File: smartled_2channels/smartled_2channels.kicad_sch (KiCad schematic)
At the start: 80 parts, among them J1 Conn_01x04, J2 Conn_01x02, SW1 SW_Push, U1 OC5028B, U2 MAX485E, U3 PY32F003F1xUx, U4 OC5864, U5 SGM2033-3.3, U6 OC5028B, U7 GS8521

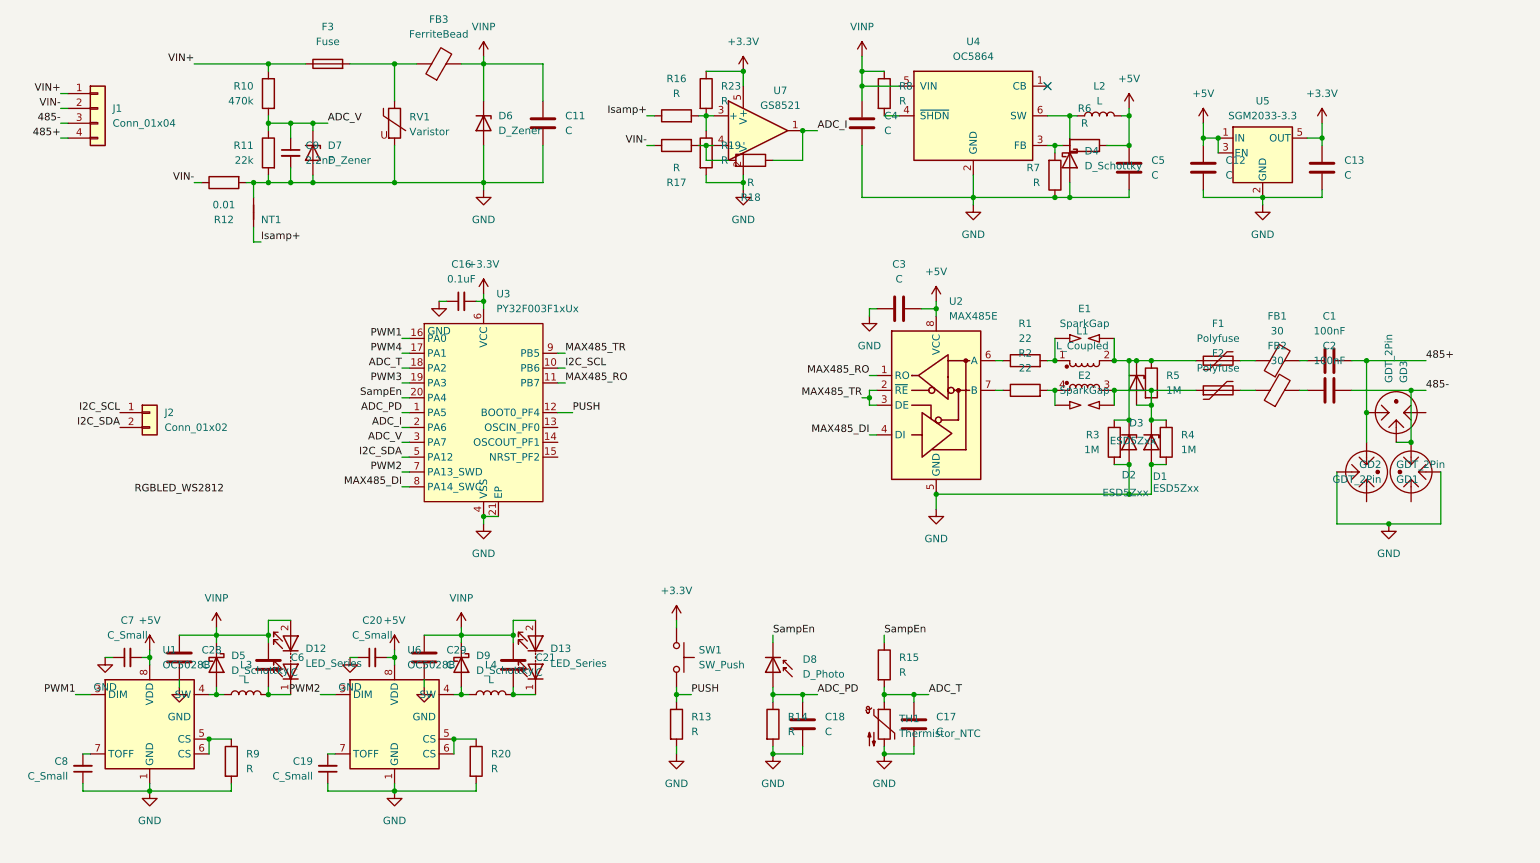
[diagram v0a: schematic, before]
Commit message: 添加麦克风声感应电路，红外和雷达传感器接口
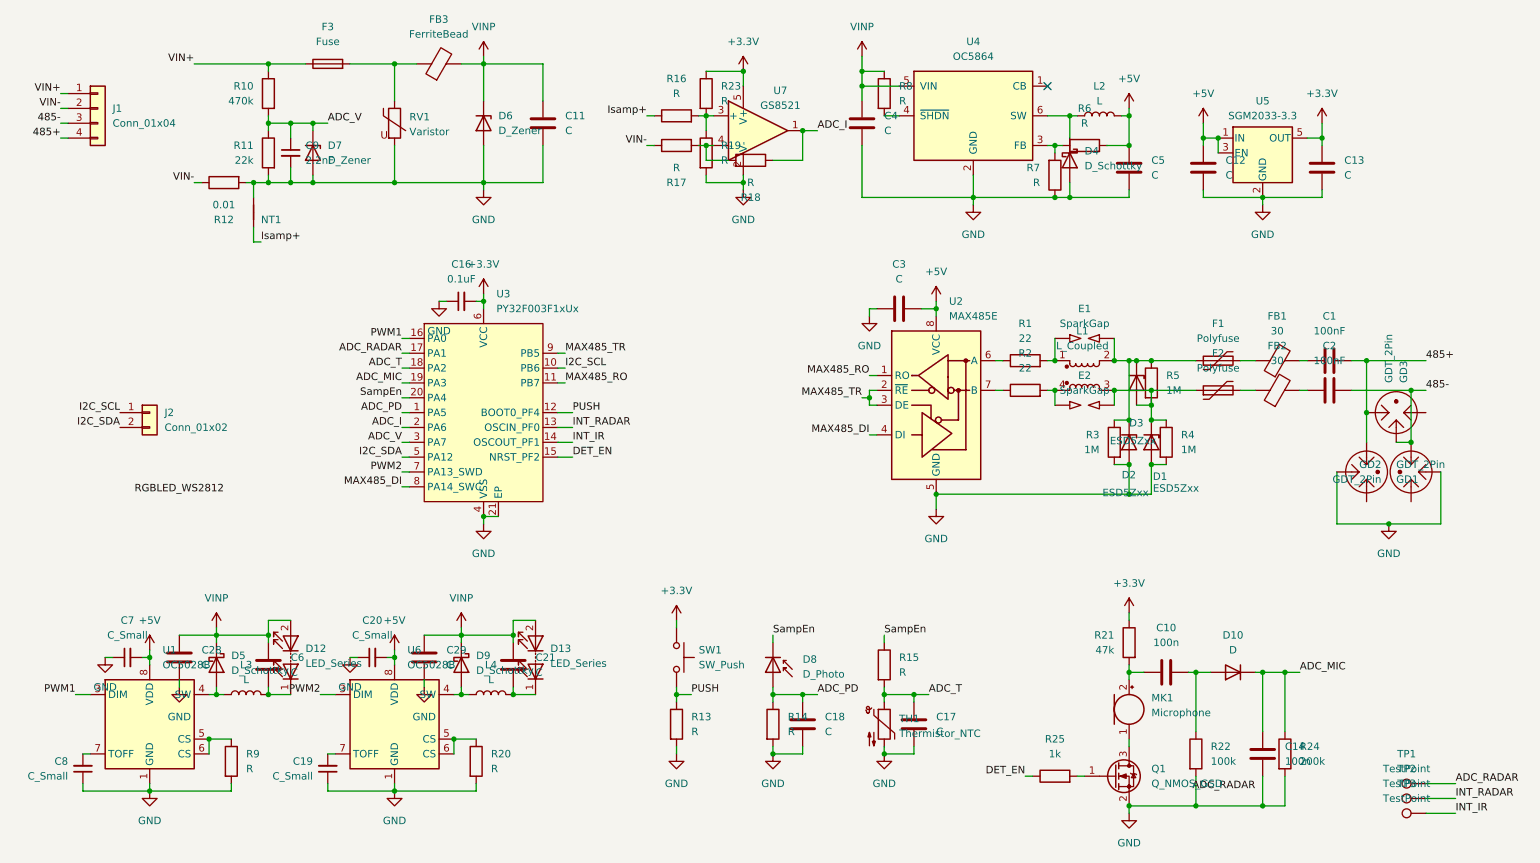
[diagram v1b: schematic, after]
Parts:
- added C10, C14: 100n, Capacitor_SMD:C_0402_1005Metric, symbol Device:C
- added D10: D, Diode_SMD:D_SOD-523, symbol Device:D
- added MK1: Microphone, Diode_SMD:D_SOD-123F, symbol Device:Microphone
- added Q1: Q_NMOS_GSD, Package_TO_SOT_SMD:SOT-23, symbol Device:Q_NMOS_GSD
- added R21: 47k, Resistor_SMD:R_0402_1005Metric, symbol Device:R
- added R22: 100k, Resistor_SMD:R_0402_1005Metric, symbol Device:R
- added R24: 200k, Resistor_SMD:R_0402_1005Metric, symbol Device:R
- added R25: 1k, Resistor_SMD:R_0402_1005Metric, symbol Device:R
- added TP1, TP2, TP3: TestPoint, TestPoint:TestPoint_Pad_D1.0mm, symbol Connector:TestPoint
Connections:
- net +3.3V: now also R21.1
- net GND: now also C14.2, Q1.2 (S), R22.2, R24.2
- net INT_RADAR: now reaches U3.13 (OSCIN_PF0)
- net INT_RADAR: now also TP2.1
- net INT_IR: now reaches U3.14 (OSCOUT_PF1)
- net INT_IR: now also TP3.1
- net DET_EN: now reaches U3.15 (NRST_PF2)
- net DET_EN: now also R25.1
- net PWM3 renamed ADC_MIC
- net ADC_MIC: now also C14.1, D10.1 (K), R24.1
- net PWM4 renamed ADC_RADAR
- net ADC_RADAR: now also TP1.1
- new net: Q1.1 (G), R25.2
- new net: C10.1, MK1.2 (+), R21.2
- new net: MK1.1 (-), Q1.3 (D)
- new net: C10.2, D10.2 (A), R22.1

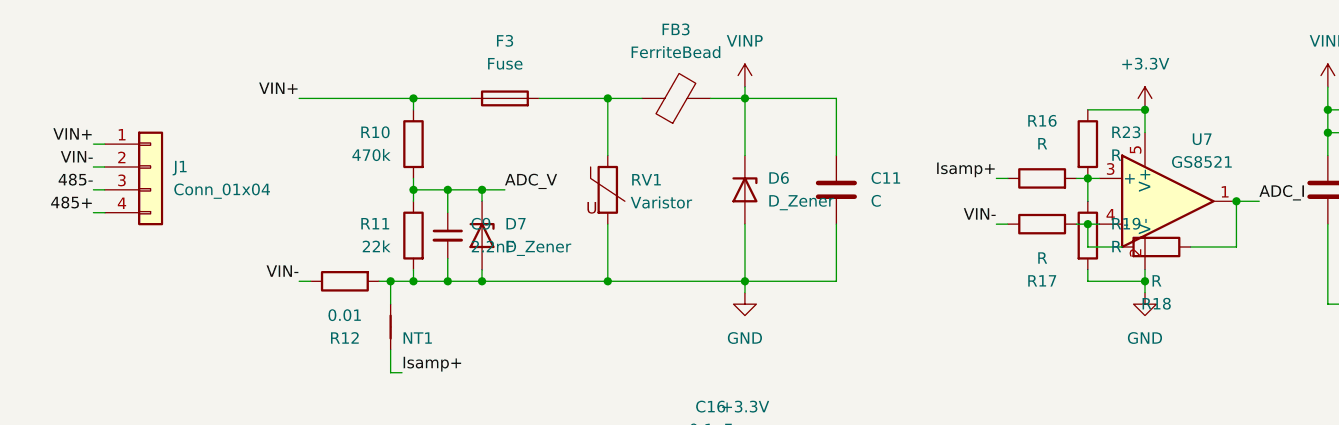
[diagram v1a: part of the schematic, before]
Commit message: 进行布线，微调原理图
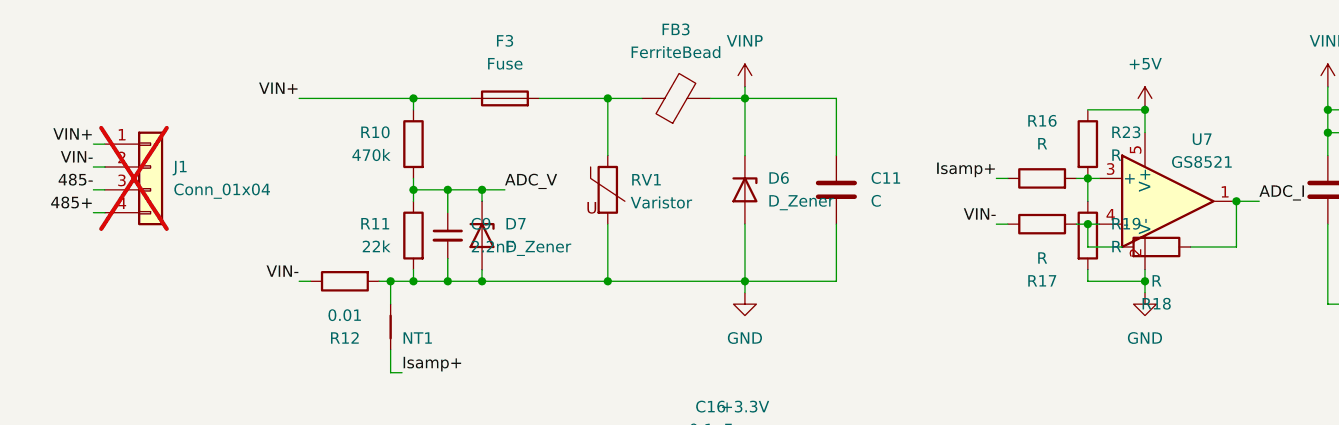
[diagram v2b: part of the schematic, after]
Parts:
- D7, MK1: footprint Diode_SMD:D_SOD-123F -> Diode_SMD:D_SOD-323
- F3: footprint project_footprints:Fuse_2410_6125Metric -> Fuse:Fuse_1206_3216Metric
- J1: now not fitted
- R22: footprint Resistor_SMD:R_0402_1005Metric -> Resistor_SMD:R_0603_1608Metric
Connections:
- net +3.3V: no longer R23.1, U7.5 (V+)
- net +5V: now also R23.1, U7.5 (V+)
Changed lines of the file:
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@@
 	)
 	(junction
-		(at 203.2 80.01)
+		(at 139.7 30.48)
 		(diameter 0)
 		(color 0 0 0 0)
 	)
 	(junction
-		(at 139.7 30.48)
+		(at 203.2 80.01)
 		(diameter 0)
 		(color 0 0 0 0)
@@
 			)
 		)
-		(property "Footprint" "Diode_SMD:D_SOD-123F"
+		(property "Footprint" "Diode_SMD:D_SOD-323"
 			(at 205.74 137.16 90)
 			(effects
@@
 			)
 		)
-		(property "Footprint" "Resistor_SMD:R_0402_1005Metric"
+		(property "Footprint" "Resistor_SMD:R_0603_1608Metric"
 			(at 215.392 147.32 90)
 			(effects
@@
 			)
 		)
-		(property "Footprint" "Diode_SMD:D_SOD-123F"
+		(property "Footprint" "Diode_SMD:D_SOD-323"
 			(at 66.04 44.45 0)
 			(effects
@@
 		(exclude_from_sim no)
 		(in_bom yes)
-		(on_board yes)
-		(dnp no)
+		(on_board no)
+		(dnp yes)
 		(fields_autoplaced yes)
 		(property "Reference" "J1"
@@
 			)
 		)
-		(property "Footprint" "project_footprints:Fuse_2410_6125Metric"
+		(property "Footprint" "Fuse:Fuse_1206_3216Metric"
 			(at 68.58 30.988 90)
 			(effects
@@
 	)
 	(symbol
+		(lib_id "power:+5V")
+		(at 139.7 30.48 0)
+		(unit 1)
+		(exclude_from_sim no)
+		(in_bom yes)
+		(on_board yes)
+		(dnp no)
+		(fields_autoplaced yes)
+		(property "Reference" "#PWR4"
+			(at 139.7 34.29 0)
+			(effects
+				(font
+					(size 1.27 1.27)
+				)
+				(hide yes)
+			)
+		)
+		(property "Value" "+5V"
+			(at 139.7 25.4 0)
+			(effects
+				(font
+					(size 1.27 1.27)
+				)
+			)
+		)
+		(property "Footprint" ""
+			(at 139.7 30.48 0)
+			(effects
+				(font
+					(size 1.27 1.27)
+				)
+				(hide yes)
+			)
+		)
+		(property "Datasheet" ""
+			(at 139.7 30.48 0)
+			(effects
+				(font
+					(size 1.27 1.27)
+				)
+				(hide yes)
+			)
+		)
+		(property "Description" "Power symbol creates a global label with name \"+5V\""
+			(at 139.7 30.48 0)
+			(effects
+				(font
+					(size 1.27 1.27)
+				)
+				(hide yes)
+			)
+		)
+		(pin "1"
+		)
+		(instances
+			(project "smartled_2channels"
+				(path "/03135fe0-800a-4910-99f5-abc1a6d2d96f"
+					(reference "#PWR4")
+					(unit 1)
+				)
+			)
+		)
+	)
+	(symbol
 		(lib_id "Device:C")
 		(at 149.86 142.24 0)
@@
 					(unit 1)
 				)
-			)
-		)
-	)
-	(symbol
-		(lib_id "power:+3.3V")
-		(at 139.7 30.48 0)
-		(unit 1)
-		(exclude_from_sim no)
-		(in_bom yes)
-		(on_board yes)
-		(dnp no)
-		(fields_autoplaced yes)
-		(property "Reference" "#PWR29"
-			(at 139.7 34.29 0)
-			(effects
-				(font
-					(size 1.27 1.27)
-				)
-				(hide yes)
-			)
-		)
-		(property "Value" "+3.3V"
-			(at 139.7 25.4 0)
-			(effects
-				(font
-					(size 1.27 1.27)
-				)
-			)
-		)
-		(property "Footprint" ""
-			(at 139.7 30.48 0)
-			(effects
-				(font
-					(size 1.27 1.27)
-				)
-				(hide yes)
-			)
-		)
-		(property "Datasheet" ""
-			(at 139.7 30.48 0)
-			(effects
-				(font
-					(size 1.27 1.27)
-				)
-				(hide yes)
-			)
-		)
-		(property "Description" "Power symbol creates a global label with name \"+3.3V\""
-			(at 139.7 30.48 0)
-			(effects
-				(font
-					(size 1.27 1.27)
-				)
-				(hide yes)
-			)
-		)
-		(pin "1"
-		)
-		(instances
-			(project "smartled_2channels"
-				(path "/03135fe0-800a-4910-99f5-abc1a6d2d96f"
-					(reference "#PWR29")
-					(unit 1)
-				)

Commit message: 修改LED输出焊盘，缩短PCB长度到83mm
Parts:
- D12, D13: footprint project_footprints:2Pads_1.0x1.5mm_P2.0mm_mpsign -> project_footprints:2Pads_1.5x2.7mm_Tshape_mpsign
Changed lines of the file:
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@@
 			)
 		)
-		(property "Footprint" "project_footprints:2Pads_1.0x1.5mm_P2.0mm_mpsign"
+		(property "Footprint" "project_footprints:2Pads_1.5x2.7mm_Tshape_mpsign"
 			(at 104.14 133.35 0)
 			(effects
@@
 			)
 		)
-		(property "Footprint" "project_footprints:2Pads_1.0x1.5mm_P2.0mm_mpsign"
+		(property "Footprint" "project_footprints:2Pads_1.5x2.7mm_Tshape_mpsign"
 			(at 62.23 133.35 0)
 			(effects

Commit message: 修复一些DRC错误，优化布线
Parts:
- NT1: footprint NetTie:NetTie-2_SMD_Pad0.5mm -> project_footprints:NetTie-2_VIA_Pad0.6_0.3mm
- U1, U6: footprint Package_SO:HSOP-8-1EP_3.9x4.9mm_P1.27mm_EP2.41x3.1mm_ThermalVias -> project_footprints:HSOP-8-1EP_3.9x4.9mm_P1.27mm_EP2.41x3.1mm_ThermalVias_0.3_0.6mm
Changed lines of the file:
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@@
 			)
 		)
-		(property "Footprint" "Package_SO:HSOP-8-1EP_3.9x4.9mm_P1.27mm_EP2.41x3.1mm_ThermalVias"
+		(property "Footprint" "project_footprints:HSOP-8-1EP_3.9x4.9mm_P1.27mm_EP2.41x3.1mm_ThermalVias_0.3_0.6mm"
 			(at 80.01 142.24 0)
 			(effects
@@
 			)
 		)
-		(property "Footprint" "NetTie:NetTie-2_SMD_Pad0.5mm"
+		(property "Footprint" "project_footprints:NetTie-2_VIA_Pad0.6_0.3mm"
 			(at 55.88 54.61 0)
 			(effects
@@
 			)
 		)
-		(property "Footprint" "Package_SO:HSOP-8-1EP_3.9x4.9mm_P1.27mm_EP2.41x3.1mm_ThermalVias"
+		(property "Footprint" "project_footprints:HSOP-8-1EP_3.9x4.9mm_P1.27mm_EP2.41x3.1mm_ThermalVias_0.3_0.6mm"
 			(at 38.1 142.24 0)
 			(effects

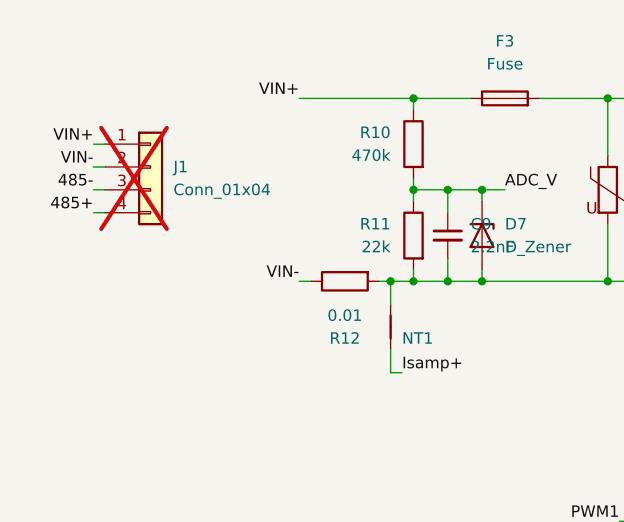
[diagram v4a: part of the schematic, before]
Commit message: 电源和通信端口放置通孔焊盘用于焊接电线
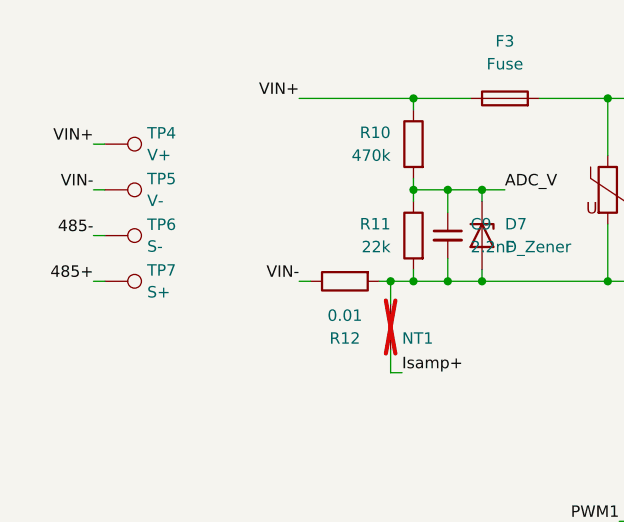
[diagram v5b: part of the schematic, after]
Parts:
- removed J1: Conn_01x04, Connector_PinHeader_2.54mm:PinHeader_1x04_P2.54mm_Vertical, symbol Connector_Generic:Conn_01x04
- added TP4: V+, TestPoint:TestPoint_THTPad_D1.0mm_Drill0.5mm, symbol Connector:TestPoint
- added TP5: V-, TestPoint:TestPoint_THTPad_D1.0mm_Drill0.5mm, symbol Connector:TestPoint
- added TP6: S-, TestPoint:TestPoint_THTPad_D1.0mm_Drill0.5mm, symbol Connector:TestPoint
- added TP7: S+, TestPoint:TestPoint_THTPad_D1.0mm_Drill0.5mm, symbol Connector:TestPoint
- NT1: now not fitted
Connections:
- net 485+: now also TP7.1
- net 485-: now also TP6.1
- net VIN+: now also TP4.1
- net VIN-: now also TP5.1
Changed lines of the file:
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@@
 	(wire
 		(pts
-			(xy 22.86 39.37) (xy 24.13 39.37)
+			(xy 22.86 44.45) (xy 24.13 44.45)
 		)
 		(stroke
@@
 	(wire
 		(pts
-			(xy 22.86 41.91) (xy 24.13 41.91)
+			(xy 22.86 49.53) (xy 24.13 49.53)
 		)
 		(stroke
@@
 	(wire
 		(pts
-			(xy 22.86 36.83) (xy 24.13 36.83)
+			(xy 22.86 39.37) (xy 24.13 39.37)
 		)
 		(stroke
@@
 	)
 	(label "485+"
-		(at 22.86 41.91 180)
+		(at 22.86 49.53 180)
 		(effects
 			(font
@@
 	)
 	(label "485-"
-		(at 22.86 39.37 180)
+		(at 22.86 44.45 180)
 		(effects
 			(font
@@
 	)
 	(label "VIN-"
-		(at 22.86 36.83 180)
+		(at 22.86 39.37 180)
 		(effects
 			(font
@@
 		(exclude_from_sim no)
 		(in_bom no)
-		(on_board yes)
-		(dnp no)
+		(on_board no)
+		(dnp yes)
 		(fields_autoplaced yes)
 		(property "Reference" "NT1"
@@
 	)
 	(symbol
+		(lib_id "Connector:TestPoint")
+		(at 24.13 39.37 270)
+		(unit 1)
+		(exclude_from_sim no)
+		(in_bom yes)
+		(on_board yes)
+		(dnp no)
+		(fields_autoplaced yes)
+		(property "Reference" "TP5"
+			(at 28.829 38.1578 90)
+			(effects
+				(font
+					(size 1.27 1.27)
+				)
+				(justify left)
+			)
+		)
+		(property "Value" "V-"
+			(at 28.829 40.5821 90)
+			(effects
+				(font
+					(size 1.27 1.27)
+				)
+				(justify left)
+			)
+		)
+		(property "Footprint" "TestPoint:TestPoint_THTPad_D1.0mm_Drill0.5mm"
+			(at 24.13 44.45 0)
+			(effects
+				(font
+					(size 1.27 1.27)
+				)
+				(hide yes)
+			)
+		)
+		(property "Datasheet" "~"
+			(at 24.13 44.45 0)
+			(effects
+				(font
+					(size 1.27 1.27)
+				)
+				(hide yes)
+			)
+		)
+		(property "Description" "test point"
+			(at 24.13 39.37 0)
+			(effects
+				(font
+					(size 1.27 1.27)
+				)
+				(hide yes)
+			)
+		)
+		(pin "1"
+		)
+		(instances
+			(project "smartled_2channels"
+				(path "/03135fe0-800a-4910-99f5-abc1a6d2d96f"
+					(reference "TP5")
+					(unit 1)
+				)
+			)
+		)
+	)
+	(symbol
 		(lib_id "power:VCC")
 		(at 160.02 27.94 0)
@@
 	)
 	(symbol
-		(lib_id "Connector_Generic:Conn_01x04")
-		(at 29.21 36.83 0)
+		(lib_id "Connector:TestPoint")
+		(at 24.13 44.45 270)
 		(unit 1)
 		(exclude_from_sim no)
 		(in_bom yes)
-		(on_board no)
-		(dnp yes)
+		(on_board yes)
+		(dnp no)
 		(fields_autoplaced yes)
-		(property "Reference" "J1"
-			(at 31.75 36.8299 0)
+		(property "Reference" "TP6"
+			(at 28.829 43.2378 90)
 			(effects
 				(font
@@
 			)
 		)
-		(property "Value" "Conn_01x04"
-			(at 31.75 39.3699 0)
+		(property "Value" "S-"
+			(at 28.829 45.6621 90)
 			(effects
 				(font
@@
 			)
 		)
-		(property "Footprint" "Connector_PinHeader_2.54mm:PinHeader_1x04_P2.54mm_Vertical"
-			(at 29.21 36.83 0)
+		(property "Footprint" "TestPoint:TestPoint_THTPad_D1.0mm_Drill0.5mm"
+			(at 24.13 49.53 0)
 			(effects
 				(font
@@
 		)
 		(property "Datasheet" "~"
-			(at 29.21 36.83 0)
+			(at 24.13 49.53 0)
 			(effects
 				(font
@@
 			)
 		)
-		(property "Description" "Generic connector, single row, 01x04, script generated (kicad-library-utils/schlib/autogen/connector/)"
-			(at 29.21 36.83 0)
+		(property "Description" "test point"
+			(at 24.13 44.45 0)
 			(effects
 				(font
@@
 		(pin "1"
 		)
-		(pin "2"
-		)
-		(pin "4"
-		)
-		(pin "3"
-		)
 		(instances
 			(project "smartled_2channels"
 				(path "/03135fe0-800a-4910-99f5-abc1a6d2d96f"
-					(reference "J1")
+					(reference "TP6")
 					(unit 1)
 				)
@@
 	)
 	(symbol
+		(lib_id "Connector:TestPoint")
+		(at 24.13 49.53 270)
+		(unit 1)
+		(exclude_from_sim no)
+		(in_bom yes)
+		(on_board yes)
+		(dnp no)
+		(fields_autoplaced yes)
+		(property "Reference" "TP7"
+			(at 28.829 48.3178 90)
+			(effects
+				(font
+					(size 1.27 1.27)
+				)
+				(justify left)
+			)
+		)
+		(property "Value" "S+"
+			(at 28.829 50.7421 90)
+			(effects
+				(font
+					(size 1.27 1.27)
+				)
+				(justify left)
+			)
+		)
+		(property "Footprint" "TestPoint:TestPoint_THTPad_D1.0mm_Drill0.5mm"
+			(at 24.13 54.61 0)
+			(effects
+				(font
+					(size 1.27 1.27)
+				)
+				(hide yes)
+			)
+		)
+		(property "Datasheet" "~"
+			(at 24.13 54.61 0)
+			(effects
+				(font
+					(size 1.27 1.27)
+				)
+				(hide yes)
+			)
+		)
+		(property "Description" "test point"
+			(at 24.13 49.53 0)
+			(effects
+				(font
+					(size 1.27 1.27)
+				)
+				(hide yes)
+			)
+		)
+		(pin "1"
+		)
+		(instances
+			(project "smartled_2channels"
+				(path "/03135fe0-800a-4910-99f5-abc1a6d2d96f"
+					(reference "TP7")
+					(unit 1)
+				)
+			)
+		)
+	)
+	(symbol
 		(lib_id "power:VCC")
 		(at 95.25 27.94 0)
@@
 					(unit 1)
 				)
+			)
+		)
+	)
+	(symbol
+		(lib_id "Connector:TestPoint")
+		(at 24.13 34.29 270)
+		(unit 1)
+		(exclude_from_sim no)
+		(in_bom yes)
+		(on_board yes)
+		(dnp no)
+		(fields_autoplaced yes)
+		(property "Reference" "TP4"
+			(at 28.829 33.0778 90)
+			(effects
+				(font
+					(size 1.27 1.27)
+				)
+				(justify left)
+			)
+		)
+		(property "Value" "V+"
+			(at 28.829 35.5021 90)
+			(effects
+				(font
+					(size 1.27 1.27)
+				)
+				(justify left)
+			)
+		)
+		(property "Footprint" "TestPoint:TestPoint_THTPad_D1.0mm_Drill0.5mm"
+			(at 24.13 39.37 0)
+			(effects
+				(font
+					(size 1.27 1.27)
+				)
+				(hide yes)
+			)
+		)
+		(property "Datasheet" "~"
+			(at 24.13 39.37 0)
+			(effects
+				(font
+					(size 1.27 1.27)
+				)
+				(hide yes)
+			)
+		)
+		(property "Description" "test point"
+			(at 24.13 34.29 0)
+			(effects
+				(font
+					(size 1.27 1.27)
+				)
+				(hide yes)
+			)
+		)
+		(pin "1"
+		)
+		(instances
+			(project ""
+				(path "/03135fe0-800a-4910-99f5-abc1a6d2d96f"
+					(reference "TP4")
+					(unit 1)
+				)
